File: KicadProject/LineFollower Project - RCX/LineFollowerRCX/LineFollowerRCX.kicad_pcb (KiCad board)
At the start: 2 copper layers, 100 x 100.6 mm, 12 parts, among them J1 Conn_01x11_Pin, J10 GND pinos, J2 Motor 1, J3 Motor 1, J4 Modulo bluetooth, J8 Conector sensor lateral Direi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, J9 VCC pinos, U1 ROB-14450, U2 LM7805_TO220

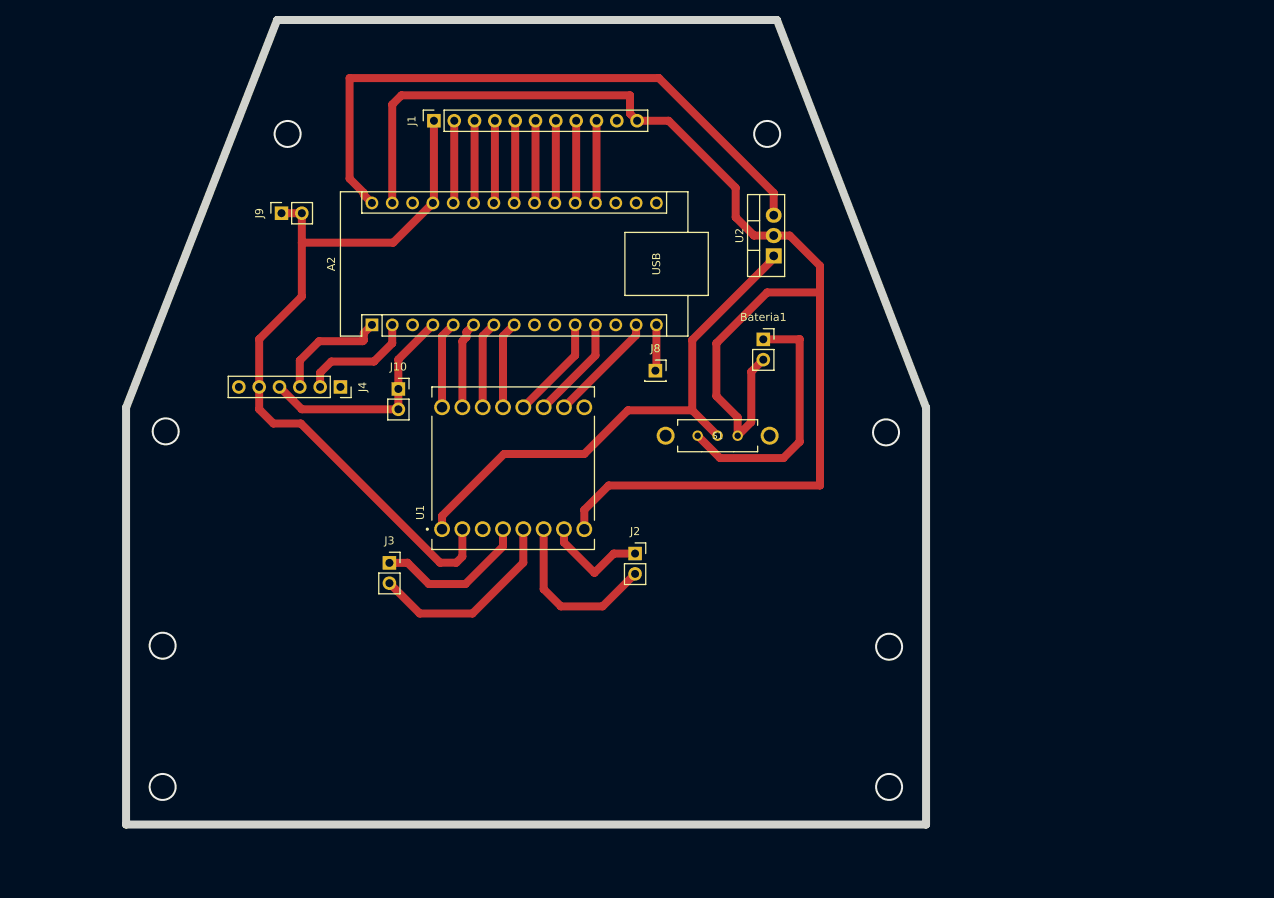
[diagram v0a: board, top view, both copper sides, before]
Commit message: altera dimensões da placa & ajusta posições dos componentes
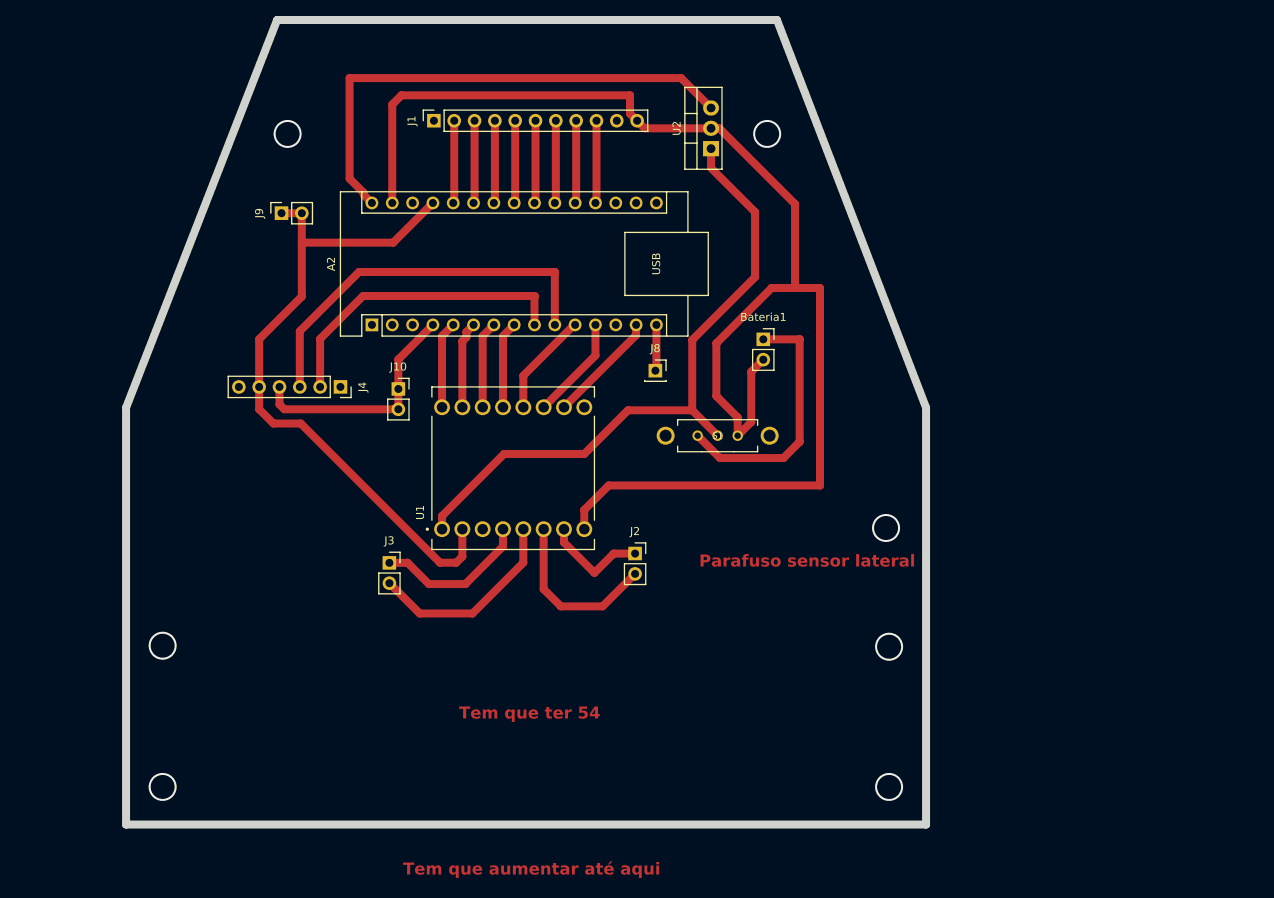
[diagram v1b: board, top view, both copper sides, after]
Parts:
- moved U2 15.5 mm to (184.5, 70.6)
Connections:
- A2 pad 1: Net-(A2-D1/TX) -> unconnected-(A2-D1/TX-Pad1)
- A2 pad 10: unconnected-(A2-D7-Pad10) -> /D7
- A2 pad 16: Net-(A2-D13) -> unconnected-(A2-D13-Pad16)
- A2 pad 2: Net-(A2-D0/RX) -> unconnected-(A2-D0/RX-Pad2)
- A2 pad 9: unconnected-(A2-D6-Pad9) -> /D6
- J4 pad 2: Net-(A2-D0/RX) -> /D6
- J4 pad 3: Net-(A2-D1/TX) -> /D7
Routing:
- net /D7: track 0.00 -> 48.6 mm
- net /D6: track 0.00 -> 38.7 mm
- net Bateria Arduino: track 78.5 -> 63.5 mm
- net Net-(U1-VM): track 66.4 -> 81.1 mm
- net Net-(A2-D1/TX): track 14.7 -> 0.00 mm
- net Net-(A2-D0/RX): track 14.6 -> 0.00 mm
- net Alimentação sensores: track 95.1 -> 85.0 mm
- net GND: track 206.6 -> 207.4 mm
- net (no net): vias 8 -> 7
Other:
- board text added: "${REFERENCE}"
- board text added: "Parafuso sensor lateral"
- board text added: "Tem que aumentar até aqui"
- board text added: "Tem que ter 54"

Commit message: fix; arrumando corte da placa
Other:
- board text removed: "${REFERENCE}"
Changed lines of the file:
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@@
 		(layer "F.Cu")
 	)
-	(gr_line
-		(start 130.259283 54.5)
-		(end 111.379 102.955)
+	(gr_poly
+		(pts
+			(xy 211.836 155.067) (xy 211.836 103) (xy 193.197717 54.5) (xy 130.716283 54.5) (xy 111.836 102.955)
+			(xy 111.836 155.067)
+		)
 		(stroke
 			(width 1)
-			(type default)
-		)
-		(layer "Edge.Cuts")
-	)
-	(gr_line
-		(start 211.379 155.067)
-		(end 211.379 103)
-		(stroke
-			(width 1)
-			(type default)
-		)
-		(layer "Edge.Cuts")
-	)
-	(gr_line
-		(start 192.740717 54.5)
-		(end 130.259283 54.5)
-		(stroke
-			(width 1)
-			(type default)
-		)
-		(layer "Edge.Cuts")
-	)
-	(gr_line
-		(start 192.740717 54.5)
-		(end 211.379 102.955)
-		(stroke
-			(width 1)
-			(type default)
-		)
-		(layer "Edge.Cuts")
-	)
-	(gr_line
-		(start 111.415565 102.963001)
-		(end 111.415565 155.067)
-		(stroke
-			(width 0.05)
-			(type default)
-		)
-		(layer "Edge.Cuts")
-	)
-	(gr_line
-		(start 111.379 155.067)
-		(end 211.379 155.067)
-		(stroke
-			(width 1)
-			(type default)
-		)
-		(layer "Edge.Cuts")
-	)
-	(gr_line
-		(start 111.379 102.955)
-		(end 111.379 155.067)
-		(stroke
-			(width 1)
-			(type default)
-		)
+			(type solid)
+		)
+		(fill none)
 		(layer "Edge.Cuts")
 	)
@@
 			)
 			(justify left bottom)
-		)
-	)
-	(gr_text "${REFERENCE}"
-		(at 100.725 45.69 90)
-		(layer "F.Fab")
-		(effects
-			(font
-				(size 1 1)
-				(thickness 0.15)
-			)
 		)
 	)
@@
 			(extension_offset 0.5) keep_text_aligned)
 	)
+	(segment
+		(start 211.379 104.318)
+		(end 211.582 104.521)
+		(width 0.2)
+		(layer "F.Cu")
+		(net 0)
+	)
 	(via
 		(at 206.756 150.368)
@@
 		(net 40)
 	)
-	(group ""
-		(members "06720ef3-821e-42ea-b7c5-097c0e2e6224")
-	)
-	(group ""
-		(members "52d19d6b-c239-4e5a-8907-7798952ffbd5")
-	)
-	(group ""
-		(members "0e81edb9-fa4b-4098-9f79-3a9d3da1dfdd")
-	)
 )

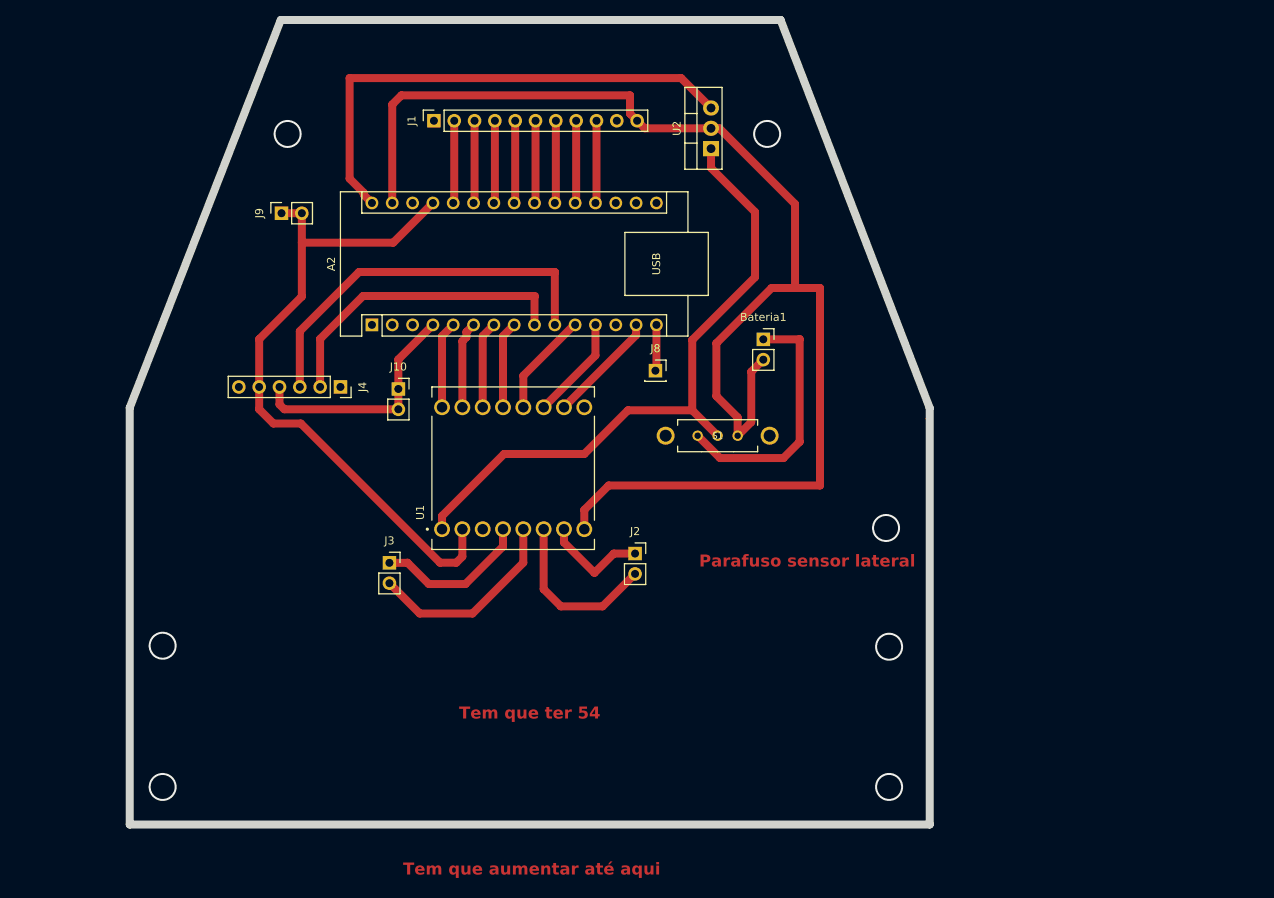
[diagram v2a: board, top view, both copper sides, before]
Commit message: fix: troca porta PWMA da ponte h para pino 10
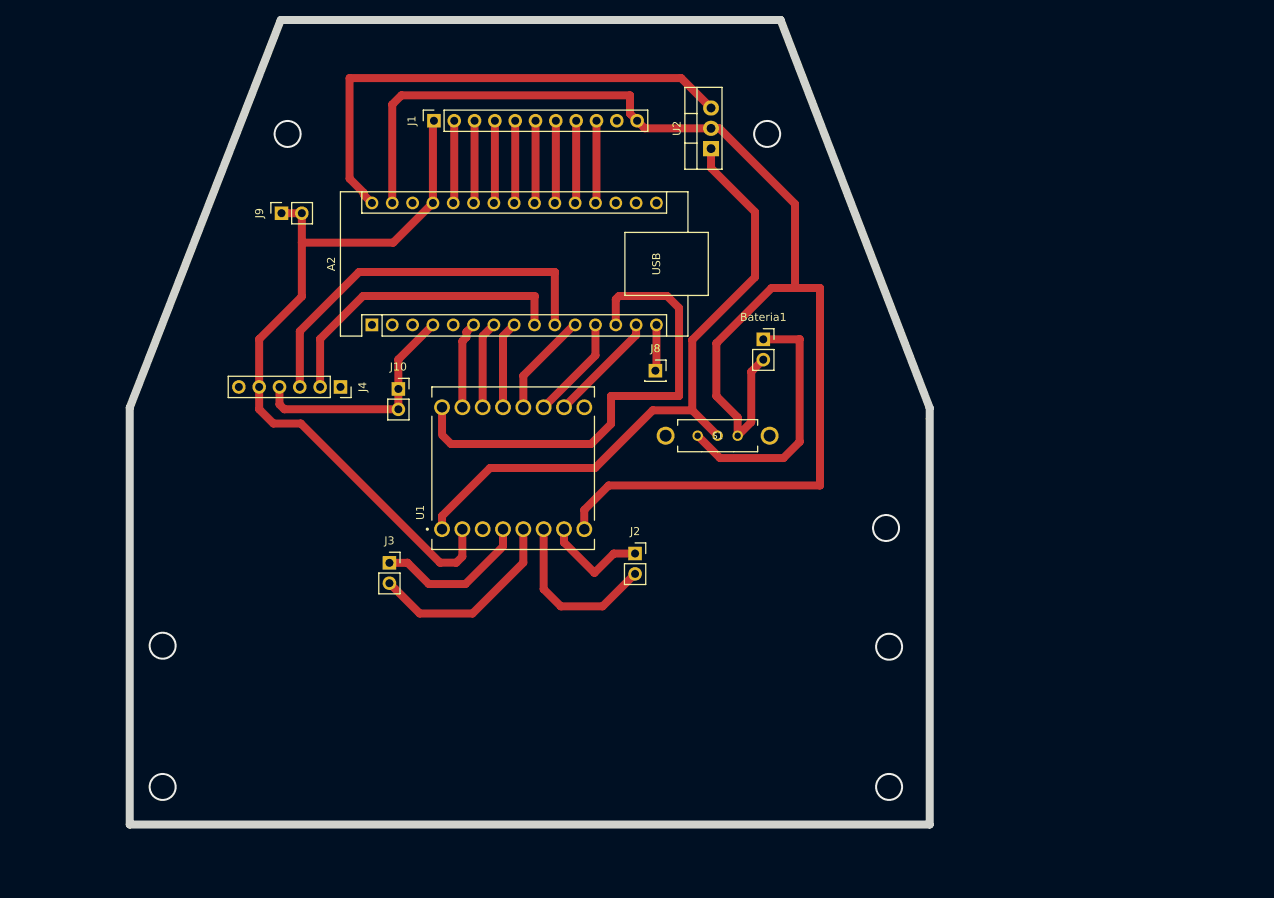
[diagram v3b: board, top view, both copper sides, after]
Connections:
- A2 pad 13: unconnected-(A2-D10-Pad13) -> Net-(A2-D10)
- A2 pad 5: Net-(A2-D2) -> unconnected-(A2-D2-Pad5)
- U1 pad 16: Net-(A2-D2) -> Net-(A2-D10)
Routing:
- net Net-(A2-D10): track 0.00 -> 61.2 mm
- net Net-(A2-D2): track 10.9 -> 0.00 mm
- net Alimentação sensores: track 85.0 -> 95.3 mm
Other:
- board text removed: "Parafuso sensor lateral"
- board text removed: "Tem que aumentar até aqui"
- board text removed: "Tem que ter 54"

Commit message: fix: arrumando espaçãmento da bateria robô
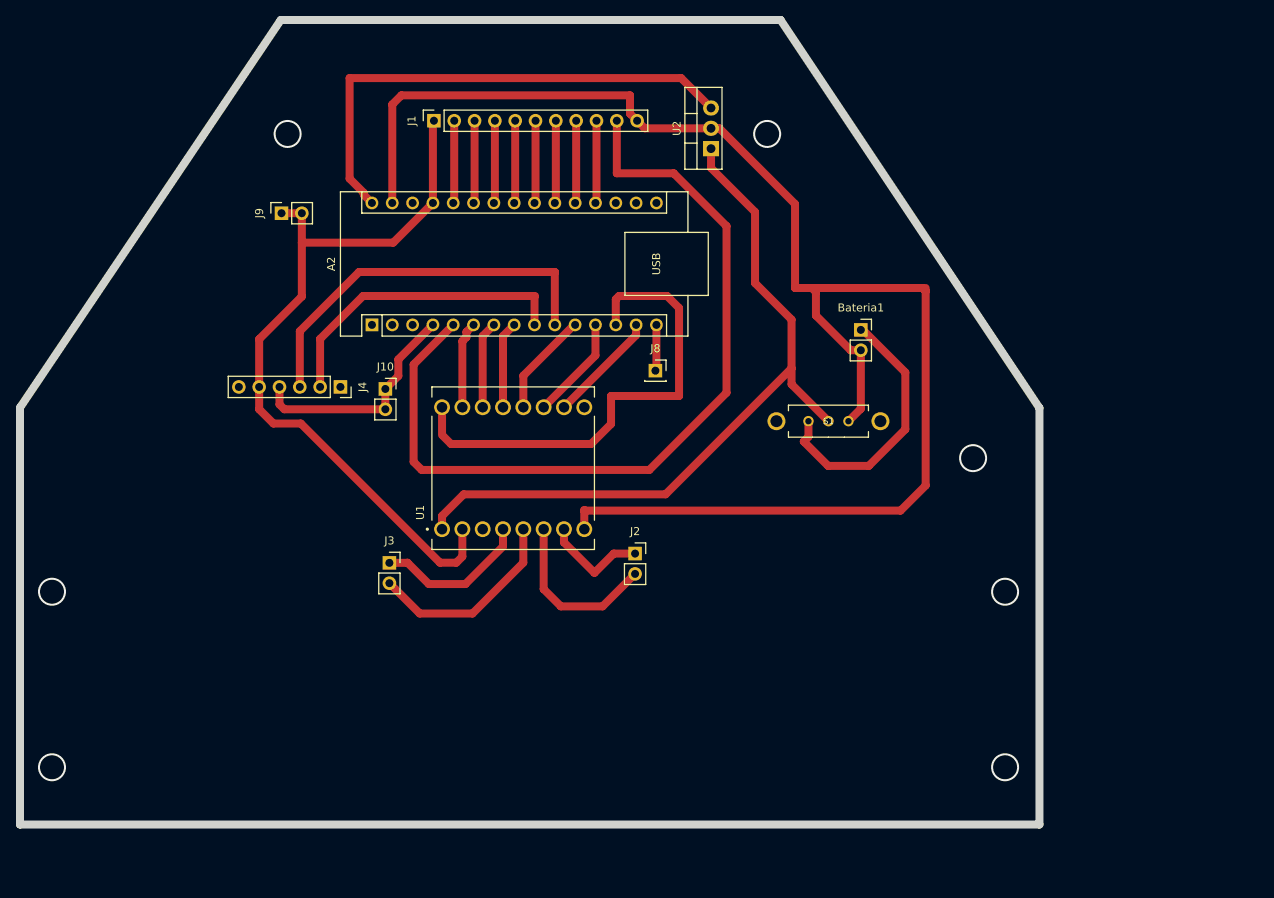
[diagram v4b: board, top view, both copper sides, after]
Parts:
- moved S1 14.0 mm to (199.2, 104.6)
- moved Bateria1 12.2 mm to (203.2, 93.2)
- moved J10 1.63 mm to (143.8, 100.6)
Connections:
- A2 pad 5: unconnected-(A2-D2-Pad5) -> Net-(A2-D2)
- J1 pad 10: unconnected-(J1-Pin_10-Pad10) -> Net-(A2-D2)
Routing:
- net Net-(A2-D2): track 0.00 -> 106.6 mm
- net Net-(U1-VM): track 81.1 -> 93.1 mm
- net GND: track 207.4 -> 217.4 mm
- net Net-(Bateria1-+): track 32.1 -> 33.5 mm
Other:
- board size 100 x 100.6 mm -> 127.4 x 100.6 mm

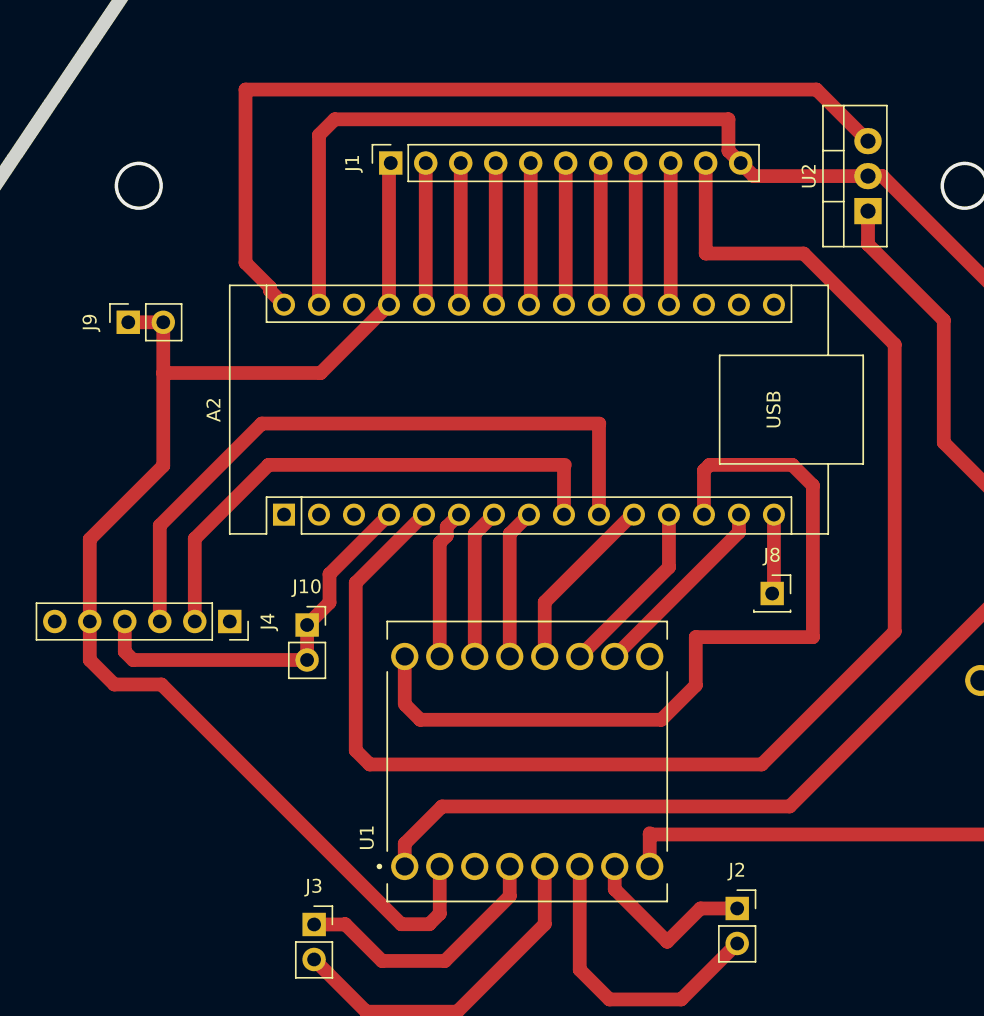
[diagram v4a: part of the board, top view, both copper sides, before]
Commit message: fix: ajusta pinos de alimentacao da ponte h e sensores
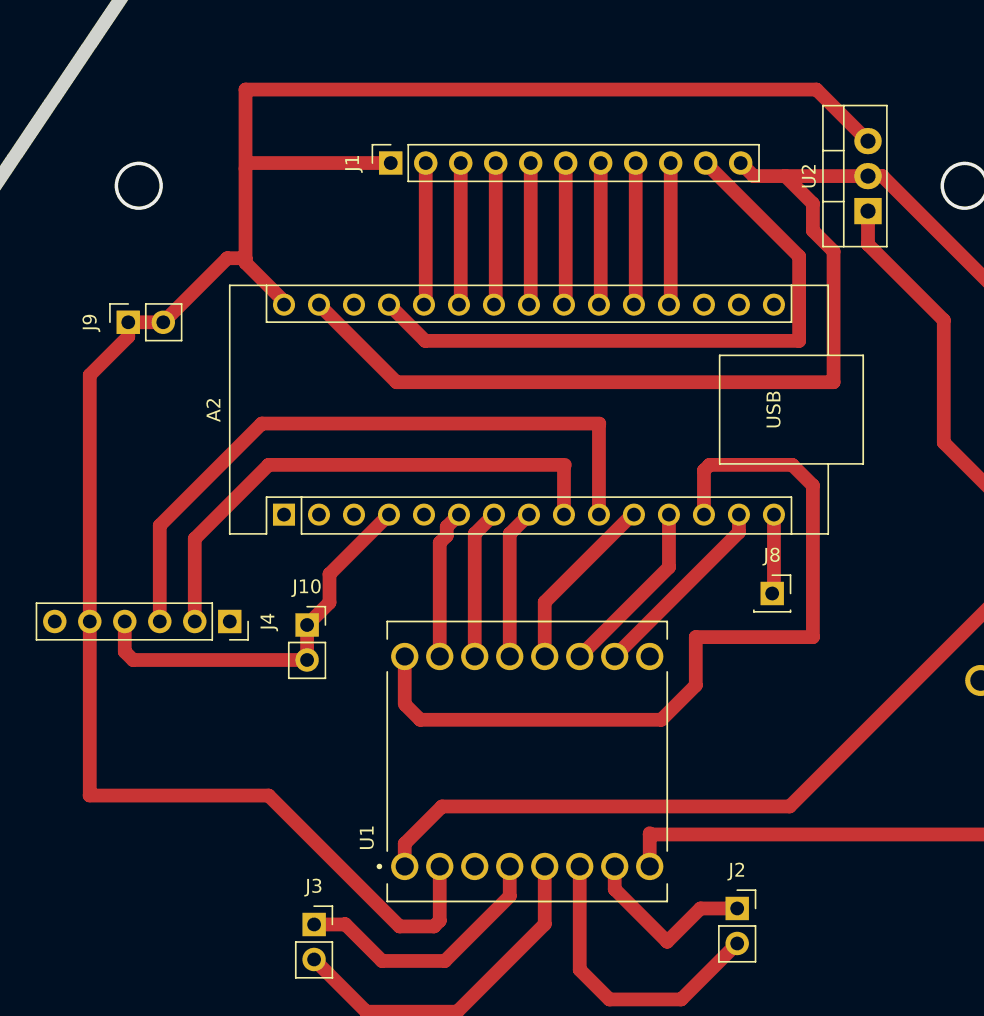
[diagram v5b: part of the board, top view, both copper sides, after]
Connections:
- A2 pad 27: Alimentação sensores -> Net-(A2-+5V)
- A2 pad 5: Net-(A2-D2) -> unconnected-(A2-D2-Pad5)
- J1 pad 1: Alimentação sensores -> Bateria Arduino
- J1 pad 10: Net-(A2-D2) -> Net-(A2-+5V)
- J4 pad 5: Alimentação sensores -> Bateria Arduino
- J9 pad 1: Alimentação sensores -> Bateria Arduino
- J9 pad 2: Alimentação sensores -> Bateria Arduino
- U1 pad 2: Alimentação sensores -> Bateria Arduino
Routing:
- net Net-(A2-D2): track 106.6 -> 0.00 mm
- net Alimentação sensores: track 95.3 -> 0.00 mm
- net Bateria Arduino: track 63.5 -> 153.6 mm
- net Net-(A2-+5V): track 0.00 -> 46.8 mm
- net GND: track 217.4 -> 227.5 mm
